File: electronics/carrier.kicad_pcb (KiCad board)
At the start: 2 copper layers, 120 x 80 mm, 21 parts, among them J1 HOST_UART_3V3, J2 SHRIKE_HARNESS, J3 HC_SR04, J4 L298N_LOGIC, J5 ESTOP_NC_LOOP, J6 SENSOR_5V_IN, U1 ISO7721DR, U2 SN74LVC1G17DBVR

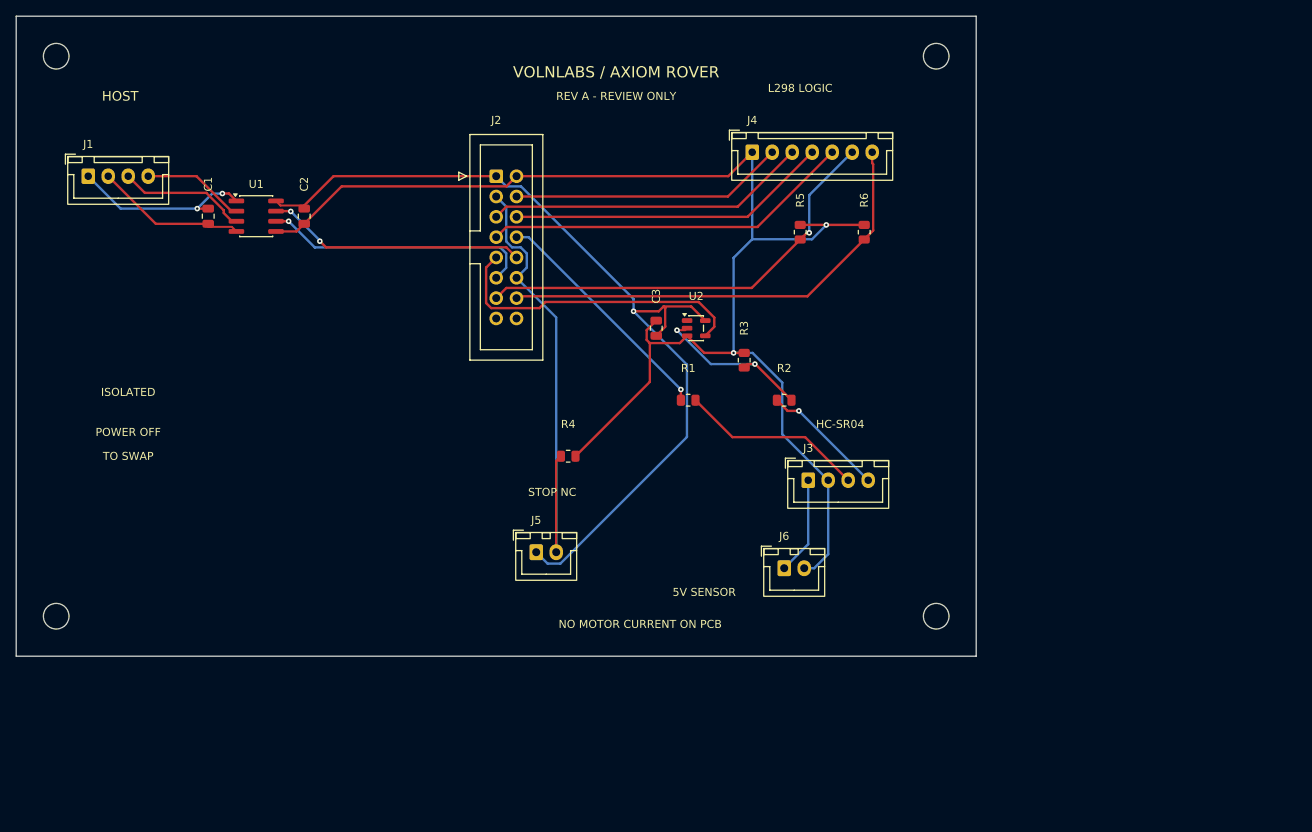
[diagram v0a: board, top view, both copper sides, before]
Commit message: Add Rev B Pi 5 and Shrike rover carrier and enclosure
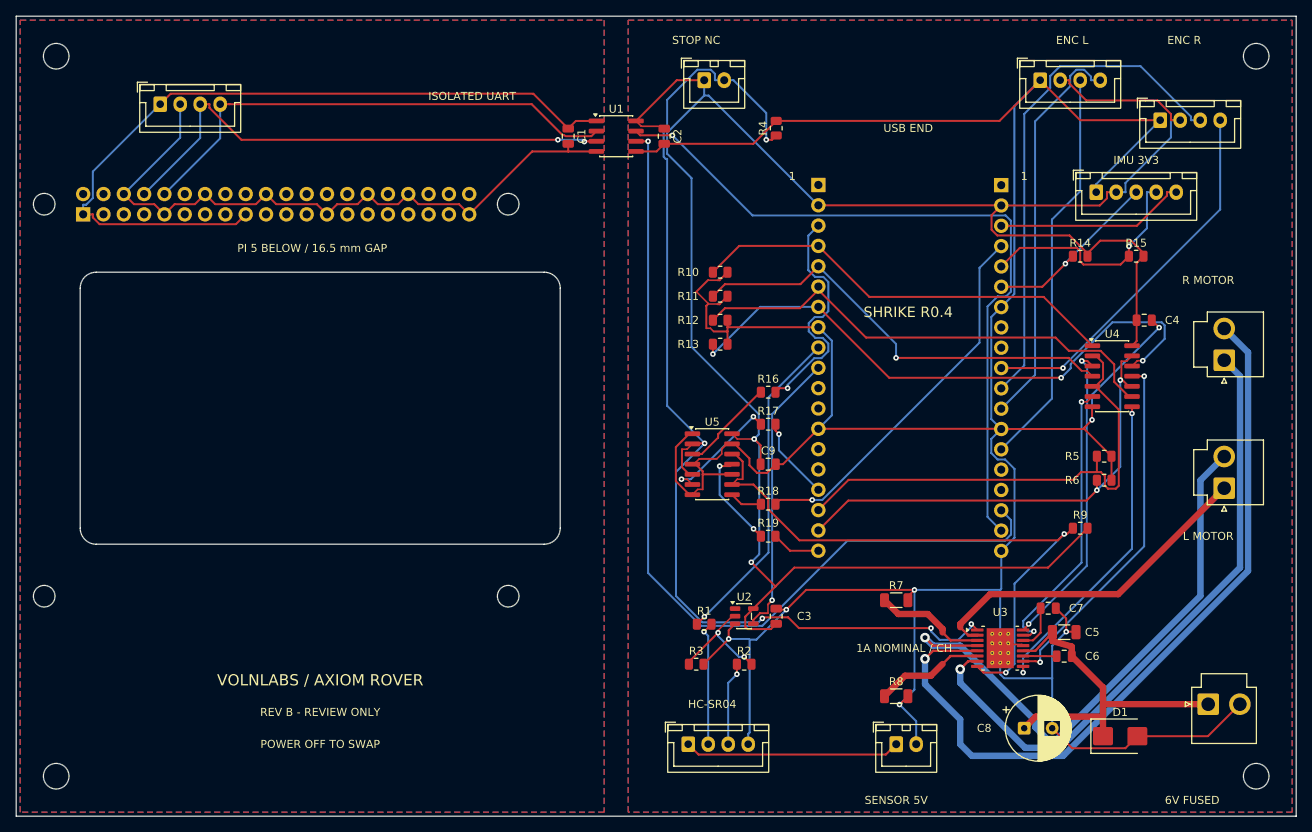
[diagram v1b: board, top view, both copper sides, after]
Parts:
- added C4: 100nF 16V X7R, Rover:C_0805_2012Metric, F.Cu at (141.0, 38.0)
- added C5: 10uF 16V X7R, Rover:C_1206_3216Metric, F.Cu at (131.0, 77.0)
- added C6: 10nF 25V X7R, Rover:C_0805_2012Metric, F.Cu at (131.0, 80.0)
- added C7: 2.2uF 16V X7R, Rover:C_0805_2012Metric, F.Cu at (129.0, 74.0)
- added C8: 470uF 16V, Rover:CP_Radial_D8.0mm_P3.50mm, F.Cu at (126.0, 89.0)
- added C9: 100nF 16V X7R, Rover:C_0805_2012Metric, F.Cu at (94.0, 56.0)
- added D1: SMBJ6.0A, Rover:D_SMB, F.Cu at (138.0, 90.0)
- added H5: M2.5 NPTH, Rover:MountingHole_2.7mm_M2.5, F.Cu at (3.50, 23.5)
- added H6: M2.5 NPTH, Rover:MountingHole_2.7mm_M2.5, F.Cu at (61.5, 23.5)
- added H7: M2.5 NPTH, Rover:MountingHole_2.7mm_M2.5, F.Cu at (3.50, 72.5)
- added H8: M2.5 NPTH, Rover:MountingHole_2.7mm_M2.5, F.Cu at (61.5, 72.5)
- added J10: ENCODER_LEFT_3V3, Rover:JST_XH_B4B-XH-A_1x04_P2.50mm_Vertical, F.Cu at (128.0, 8.00)
- added J11: ENCODER_RIGHT_3V3, Rover:JST_XH_B4B-XH-A_1x04_P2.50mm_Vertical, F.Cu at (143.0, 13.0)
- added J12: ALTERNATE_HOST_UART, Rover:JST_XH_B4B-XH-A_1x04_P2.50mm_Vertical, F.Cu at (18.0, 11.0)
- added J13: IMU_3V3_I2C_INT, Rover:JST_XH_B5B-XH-A_1x05_P2.50mm_Vertical, F.Cu at (135.0, 22.0)
- added J7: 6V_AFTER_FUSE_AND_STOP_RELAY, Rover:JST_VH_B2P-VH_1x02_P3.96mm_Vertical, F.Cu at (149.0, 86.0)
- added J8: LEFT_MOTOR, Rover:JST_VH_B2P-VH_1x02_P3.96mm_Vertical, F.Cu at (151.0, 59.0)
- added J9: RIGHT_MOTOR, Rover:JST_VH_B2P-VH_1x02_P3.96mm_Vertical, F.Cu at (151.0, 43.0)
- added R10: 10k 1%, Rover:R_0805_2012Metric, F.Cu at (88.0, 32.0)
- added R11: 10k 1%, Rover:R_0805_2012Metric, F.Cu at (88.0, 35.0)
- added R12: 10k 1%, Rover:R_0805_2012Metric, F.Cu at (88.0, 38.0)
- added R13: 10k 1%, Rover:R_0805_2012Metric, F.Cu at (88.0, 41.0)
- added R14: 4.7k 1%, Rover:R_0805_2012Metric, F.Cu at (133.0, 30.0)
- added R15: 4.7k 1%, Rover:R_0805_2012Metric, F.Cu at (140.0, 30.0)
- added R16: 1k 1%, Rover:R_0805_2012Metric, F.Cu at (94.0, 47.0)
- added R17: 1k 1%, Rover:R_0805_2012Metric, F.Cu at (94.0, 51.0)
- added R18: 1k 1%, Rover:R_0805_2012Metric, F.Cu at (94.0, 61.0)
- added R19: 1k 1%, Rover:R_0805_2012Metric, F.Cu at (94.0, 65.0)
- added R7: 0.20R 1W CSRT1206FTR200, Rover:R_1206_3216Metric, F.Cu at (110.0, 73.0)
- added R8: 0.20R 1W CSRT1206FTR200, Rover:R_1206_3216Metric, F.Cu at (110.0, 85.0)
- added R9: 10k 1%, Rover:R_0805_2012Metric, F.Cu at (133.0, 64.0)
- added U3: DRV8833PWPR, Rover:HTSSOP-16-1EP_4.4x5mm_P0.65mm_EP3.4x5mm_Mask2.46x2.31mm_ThermalVias, F.Cu at (123.0, 79.0)
- added U4: SN74LVC08ADR, Rover:SOIC-14_3.9x8.7mm_P1.27mm, F.Cu at (137.0, 45.0)
- added U5: SN74LVC125ADR, Rover:SOIC-14_3.9x8.7mm_P1.27mm, F.Cu at (87.0, 56.0)
- J1: value HOST_UART_3V3 -> ESQ-120-24-G-D_PI5_BOTTOM; footprint Rover:JST_XH_B4B-XH-A_1x04_P2.50mm_Vertical -> Rover:Pi5_Socket_2x20; moved to B.Cu
- J2: value SHRIKE_HARNESS -> SHRIKE_J2_SSW-119-01-G-S; footprint Rover:IDC-Header_2x08_P2.54mm_Vertical -> Rover:SSW-119-01-G-S
- J3: value HC_SR04 -> HC_SR04_VCC_TRIG_ECHO_GND
- J4: value L298N_LOGIC -> SHRIKE_J4_SSW-119-01-G-S; footprint Rover:JST_XH_B7B-XH-A_1x07_P2.50mm_Vertical -> Rover:SSW-119-01-G-S
- J5: value ESTOP_NC_LOOP -> ESTOP_LOGIC_NC
- J6: value SENSOR_5V_IN -> BASE_SENSOR_5V_IN
- moved J5 62.6 mm to (86.0, 8.00)
- moved R4 48.5 mm to (95.0, 14.0), turned to 90 degrees
- moved R5 47.2 mm to (136.0, 55.0), turned to 0 degrees
- moved C1 46.1 mm to (69.0, 15.0)
- moved C2 46.1 mm to (81.0, 15.0)
- moved U1 46.1 mm to (75.0, 15.0)
- moved H3 44.7 mm to (155.0, 95.0)
- moved R6 43.1 mm to (136.0, 58.0), turned to 0 degrees
- moved J2 40.3 mm to (100.3, 21.1)
- moved H2 40.0 mm to (155.0, 5.00)
- moved C3 39.0 mm to (95.0, 75.0)
- moved R3 38.5 mm to (85.0, 81.0), turned to 0 degrees
- moved U2 36.5 mm to (91.0, 75.0)
- moved J3 36.2 mm to (84.0, 91.0)
- moved R2 33.4 mm to (91.0, 81.0)
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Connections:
- J1 pad 2: /H_GND -> unconnected-(J1-Pad2)
- J1 pad 3: /H_TX -> unconnected-(J1-Pad3)
- J1 pad 4: /H_RX -> unconnected-(J1-Pad4)
- J2 pad 1: /BASE_3V3 -> unconnected-(J2-Pad1)
- J2 pad 10: /RP_UART_TX -> /US_ECHO_3V
- J2 pad 11: /RP_UART_RX -> unconnected-(J2-Pad11)
- J2 pad 12: /ESTOP_N -> unconnected-(J2-Pad12)
- J2 pad 13: /FPGA_PWM_L -> /BASE_GND
- J2 pad 14: /FPGA_PWM_R -> unconnected-(J2-Pad14)
- J2 pad 16: unconnected-(J2-Pad16) -> /ESTOP_FPGA
- J2 pad 2: /BASE_GND -> /BASE_3V3
- J2 pad 3: /ESTOP_N -> /ESTOP_RP
- J2 pad 8: /US_TRIG -> /BASE_GND
- J2 pad 9: /US_ECHO_3V -> /US_TRIG
- J3 pad 2: /BASE_GND -> /SENSOR_TRIG
- J3 pad 3: /SENSOR_TRIG -> /US_ECHO_5V
- J3 pad 4: /US_ECHO_5V -> /BASE_GND
- J4 pad 1: /BASE_GND -> unconnected-(J4-Pad1)
- J4 pad 2: /L_IN1 -> /BASE_3V3
- J4 pad 3: /L_IN2 -> /IMU_INT
- J4 pad 4: /R_IN3 -> /FAULT_RP_N
- J4 pad 5: /R_IN4 -> /IMU_SCL
- J4 pad 6: /FPGA_PWM_L -> /IMU_SDA
- J4 pad 7: /FPGA_PWM_R -> /BASE_GND
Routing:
- net /BASE_GND: track 177.4 -> 452.3 mm, vias 2 -> 7
- net /BASE_3V3: track 113.4 -> 273.6 mm, vias 1 -> 2
- net /MOTOR_R_N: track 0.00 -> 97.1 mm, vias 0 -> 1
- net /MOTOR_R_P: track 0.00 -> 78.7 mm, vias 0 -> 1
- net /RP_UART_RX: track 34.0 -> 111.8 mm
- net /DRV_FAULT_N: track 0.00 -> 76.6 mm, vias 0 -> 2
- net /ESTOP_N: track 61.5 -> 136.5 mm, vias 0 -> 5
- net /HOST_3V3: track 22.7 -> 96.8 mm, vias 2 -> 0
- net /MOTOR_L_N: track 0.00 -> 73.2 mm, vias 0 -> 1
- net /H_GND: track 19.1 -> 84.8 mm
- net /ENC_R_A: track 0.00 -> 63.9 mm
- net /RP_UART_TX: track 32.5 -> 92.8 mm, vias 2 -> 1
- net /ENC_L_A: track 0.00 -> 50.2 mm
- net /H_RX: track 12.8 -> 63.1 mm
- net /ENC_L_B: track 0.00 -> 50.0 mm
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- added copper zone on B.Cu, net /BASE_GND
- added copper zone on F.Cu, net /BASE_GND
- added copper zone on B.Cu, net /H_GND
- added copper zone on F.Cu, net /H_GND
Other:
- board size 120 x 80 mm -> 160 x 100 mm
- board text added: "1"
- board text added: "1A NOMINAL / CH"
- board text added: "6V FUSED"
- board text added: "ENC L"
- board text added: "ENC R"
- board text added: "IMU 3V3"
- board text added: "ISOLATED UART"
- board text added: "L MOTOR"
- board text added: "PI 5 BELOW / 16.5 mm GAP"
- board text added: "POWER OFF TO SWAP"
- board text added: "R MOTOR"
- board text added: "REV B - REVIEW ONLY"
- board text added: "SENSOR 5V"
- board text added: "SHRIKE R0.4"
- board text added: "USB END"
- board text removed: "5V SENSOR"
- board text removed: "HOST"
- board text removed: "ISOLATED"
- board text removed: "L298 LOGIC"
- board text removed: "NO MOTOR CURRENT ON PCB"
- board text removed: "POWER OFF"
- board text removed: "REV A - REVIEW ONLY"
- board text removed: "TO SWAP"

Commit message: feat(pcb): improve Rev B.1 reliability and serviceability
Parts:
- added FID1: Fiducial, Rover:Fiducial_1mm_Mask3mm, F.Cu at (12.0, 6.00)
- added FID2: Fiducial, Rover:Fiducial_1mm_Mask3mm, F.Cu at (151.0, 72.0)
- added FID3: Fiducial, Rover:Fiducial_1mm_Mask3mm, F.Cu at (78.5, 95.5)
- added TP1: HOST_3V3, Rover:TestPoint_Pad_D1.5mm, F.Cu at (63.0, 11.0)
- added TP10: SENSE_R, Rover:TestPoint_Pad_D1.5mm, F.Cu at (117.0, 86.5)
- added TP2: H_GND, Rover:TestPoint_Pad_D1.5mm, F.Cu at (63.0, 16.0)
- added TP3: BASE_3V3, Rover:TestPoint_Pad_D1.5mm, F.Cu at (82.0, 22.0)
- added TP4: BASE_5V, Rover:TestPoint_Pad_D1.5mm, F.Cu at (101.0, 91.0)
- added TP5: MOTOR_6V, Rover:TestPoint_Pad_D1.5mm, F.Cu at (144.0, 76.0)
- added TP6: BASE_GND, Rover:TestPoint_Pad_D1.5mm, F.Cu at (109.0, 81.0)
- added TP7: ESTOP_N, Rover:TestPoint_Pad_D1.5mm, F.Cu at (82.0, 28.0)
- added TP8: DRV_FAULT_N, Rover:TestPoint_Pad_D1.5mm, F.Cu at (109.0, 86.0)
- added TP9: SENSE_L, Rover:TestPoint_Pad_D1.5mm, F.Cu at (117.0, 71.5)
- moved R7 6.04 mm to (115.5, 75.5), turned to 180 degrees
- moved R8 6.04 mm to (115.5, 82.5), turned to 180 degrees
- moved C6 3.84 mm to (128.0, 82.4), turned to -90 degrees
- moved C5 2.62 mm to (129.8, 79.3)
- moved C7 2.11 mm to (128.8, 76.1)
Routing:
- net /DRV_BIN1: track 39.6 -> 94.4 mm
- net /DRV_BIN2: track 44.8 -> 75.6 mm, vias 2 -> 0
- net /MOTOR_R_N: track 97.1 -> 69.2 mm
- net /BASE_3V3: track 273.6 -> 248.8 mm, vias 2 -> 7
- net /RP_UART_RX: track 111.8 -> 88.0 mm
- net /MOTOR_L_N: track 73.2 -> 53.6 mm
- net /ESTOP_N: track 136.5 -> 123.2 mm, vias 5 -> 3
- net /R_IN4: track 74.3 -> 61.3 mm, vias 3 -> 1
- net /MOTOR_R_P: track 78.7 -> 65.7 mm
- net /FPGA_PWM_L: track 62.2 -> 52.6 mm
- net /MOTOR_6V: track 44.7 -> 53.3 mm, vias 0 -> 3
- net /DRV_FAULT_N: track 76.6 -> 83.9 mm, vias 2 -> 4
- net /L_IN2: track 55.7 -> 61.8 mm, vias 1 -> 0
- net /US_ECHO_5V: track 10.5 -> 16.2 mm
- net /BASE_GND: track 452.3 -> 457.9 mm, vias 7 -> 6
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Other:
- board text added: "1:3V3 2:HG 3:TX 4:RX"
- board text added: "4:SCL 5:INT"
- board text added: "BASE_3V3"
- board text added: "BASE_5V"
- board text added: "BASE_GND"
- board text added: "DRV_FAULT_N"
- board text added: "ESTOP_N"
- board text added: "HOST_3V3"
- board text added: "H_GND"
- board text added: "J1 PI BELOW"
- board text added: "J10 1:G 2:3V3 3:A 4:B"
- board text added: "J11 1:G 2:3V3 3:A 4:B"
- board text added: "J12 ALT HOST"
- board text added: "J13 1:G 2:3V3 3:SDA"
- board text added: "J2"
- board text added: "J3 1:5V 2:T 3:E 4:G"
- board text added: "J4"
- board text added: "J5 1:3V3 2:STOP"
- board text added: "J6 1:+5V 2:G"
- board text added: "J7 1:+6V 2:G"
- board text added: "J8 1:L+ 2:L-"
- board text added: "J9 1:R+ 2:R-"
- board text added: "MOTOR_6V"
- board text added: "REV B.1 - REVIEW ONLY"
- board text added: "SENSE_L"
- board text added: "SENSE_R"
- board text removed: "REV B - REVIEW ONLY"
